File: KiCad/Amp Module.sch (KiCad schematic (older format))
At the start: 7 parts, among them J1 IDC34, J2 IDC34, J3 IDC34

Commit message: changed 4053 to DG419 & added negative latch
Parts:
- removed U?: CD4053B, symbol Analog_Switch:CD4053B
- added R? (x2): 2.2k, symbol Device:R_Small
- added R? (x2): 1k, symbol Device:R_Small
- added U? (x2): DG419, Package_SO:SOIC-8_3.9x4.9mm_P1.27mm, symbol Analog_Switch:DG419LDY
- added U? (x2): DG419LDY_Maxim, Package_SO:SOIC-8_3.9x4.9mm_P1.27mm, symbol Analog_Switch:DG419LDY_Maxim
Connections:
- wire segments 73 -> 85
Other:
- note added: "0"
- note added: "1"
- note removed: "S1=0"
- note removed: "S1=1"
- note removed: "S2=0"
- note removed: "S2=1"
- moved on the sheet: U?A, U?B, U?C

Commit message: first commit
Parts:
- removed U? (x2): DG419, Package_SO:SOIC-8_3.9x4.9mm_P1.27mm, symbol Analog_Switch:DG419LDY
- added C? (x2): 22u, symbol Device:C_Small
- added C? (x2): 22p, symbol Device:C_Small
- added R? (x2): 22K, symbol Device:R_Small
- added R? (x4): R_Small, symbol Device:R_Small
- added R? (x19): 0, symbol Device:R_Small
- added U? (x3): Opamp_Dual_Generic, symbol Device:Opamp_Dual_Generic
- added U? (x2): Rotary_SW10, symbol AmpModule:Rotary_SW10
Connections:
- wire segments 85 -> 159
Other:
- note removed: "0"
- note removed: "1"
- moved on the sheet: R?, U?A, U?B, U?C

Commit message: first single IDC commit
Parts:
- removed J3: IDC34, symbol Connector_Generic:Conn_02x17_Odd_Even
- removed U? (x2): DG419LDY_Maxim, Package_SO:SOIC-8_3.9x4.9mm_P1.27mm, symbol Analog_Switch:DG419LDY_Maxim
- removed U?: Opamp_Dual_Generic, symbol Device:Opamp_Dual_Generic
- added U? (x3): 74LS08, symbol 74xx:74LS08
- J1: value IDC34 -> DSP
- J2: value IDC34 -> LITEMOD
- U? (x2): symbol AmpModule:Rotary_SW10 -> Amp-Module-rescue:Rotary_SW10-AmpModule
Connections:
- net labels added: IOUT1MON, IOUT2MON, PROTECT1, PROTECT2, READY1, READY2, TEMPMON12, VOUT1MON, VOUT2MON
- net labels removed: DSP_IOUT1MON, DSP_IOUT2MON, DSP_PROTECT13, DSP_PROTECT24, DSP_READY13, DSP_READY24, DSP_TEMPMON12, DSP_VOUT1MON, DSP_VOUT2MON, LM_IN3+, LM_IN3-, LM_IN4+, LM_IN4-, LM_IOUT1MON, LM_IOUT2MON, LM_IOUT3MON, LM_IOUT4MON, LM_MUTE3, LM_MUTE4, LM_PROTECT1, LM_PROTECT2, LM_PROTECT3, LM_PROTECT4, LM_READY1, LM_READY2, LM_READY3, LM_READY4, LM_TEMPMON12, LM_TEMPMON34, LM_VOUT1MON, LM_VOUT2MON, LM_VOUT3MON, LM_VOUT4MON, RESERVED_A1, RESERVED_A2, RESERVED_B1, RESERVED_B2
- wire segments 159 -> 146
- no-connect marks 0 -> 4
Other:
- note added: "AUDIO"
- note added: "IDC"
- note added: "MUTE"
- note added: "TODO:\n - Check PROTECT voltage level\n - Bypass caps\n - Duplicate temp detector"
- note removed: "DSP IDC"
- note removed: "LITEMOD IDC"
- note removed: "TODO:\n - Check PROTECT voltage level\n - Bypass caps\n - VU meter"
- moved on the sheet: C?, J1, J2, R?, U?A, U?B

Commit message: freeze at 3 leds
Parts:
- removed R? (x19): 0, symbol Device:R_Small
- removed R?: R_Small, symbol Device:R_Small
- removed U? (x2): Rotary_SW10, symbol Amp-Module-rescue:Rotary_SW10-AmpModule
- added C? (x2): 22u, symbol Device:C_Small
- added R? (x2): 4.7k, symbol Device:R_Small
- added R? (x3): 18k, symbol Device:R_Small
- added R? (x2): 10k, symbol Device:R_Small
- added R? (x2): 27k, symbol Device:R_Small
- added R? (x2): 39k, symbol Device:R_Small
- added R? (x2): 53.6k, symbol Device:R_Small
- added RS? (x2): Rotary_SW07, symbol Amp-Module-rescue:Rotary_SW07
- R? (x2): value 2.2k -> 8.2k
- R? (x2): value 1k -> 2.7k
- R? (x2): value 22K -> 22k
- R? (x2): value R_Small -> 10k
- R?: value R_Small -> 18k
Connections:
- wire segments 146 -> 125
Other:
- moved on the sheet: R?, U?A, U?B

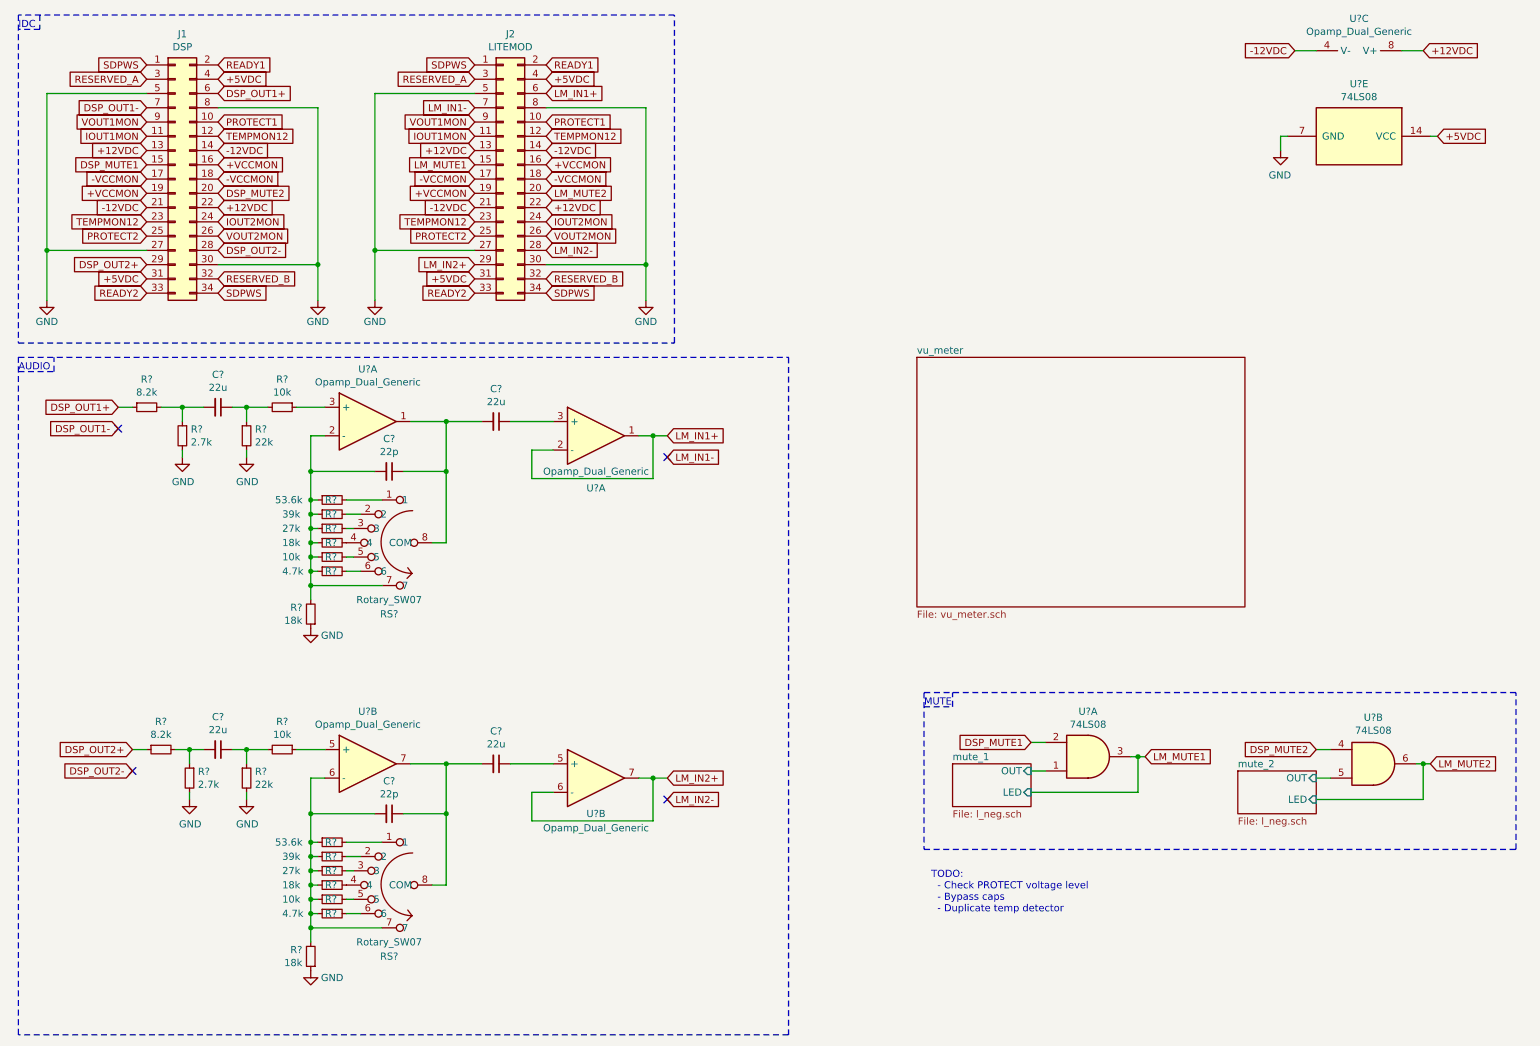
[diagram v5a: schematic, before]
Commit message: schematic completed
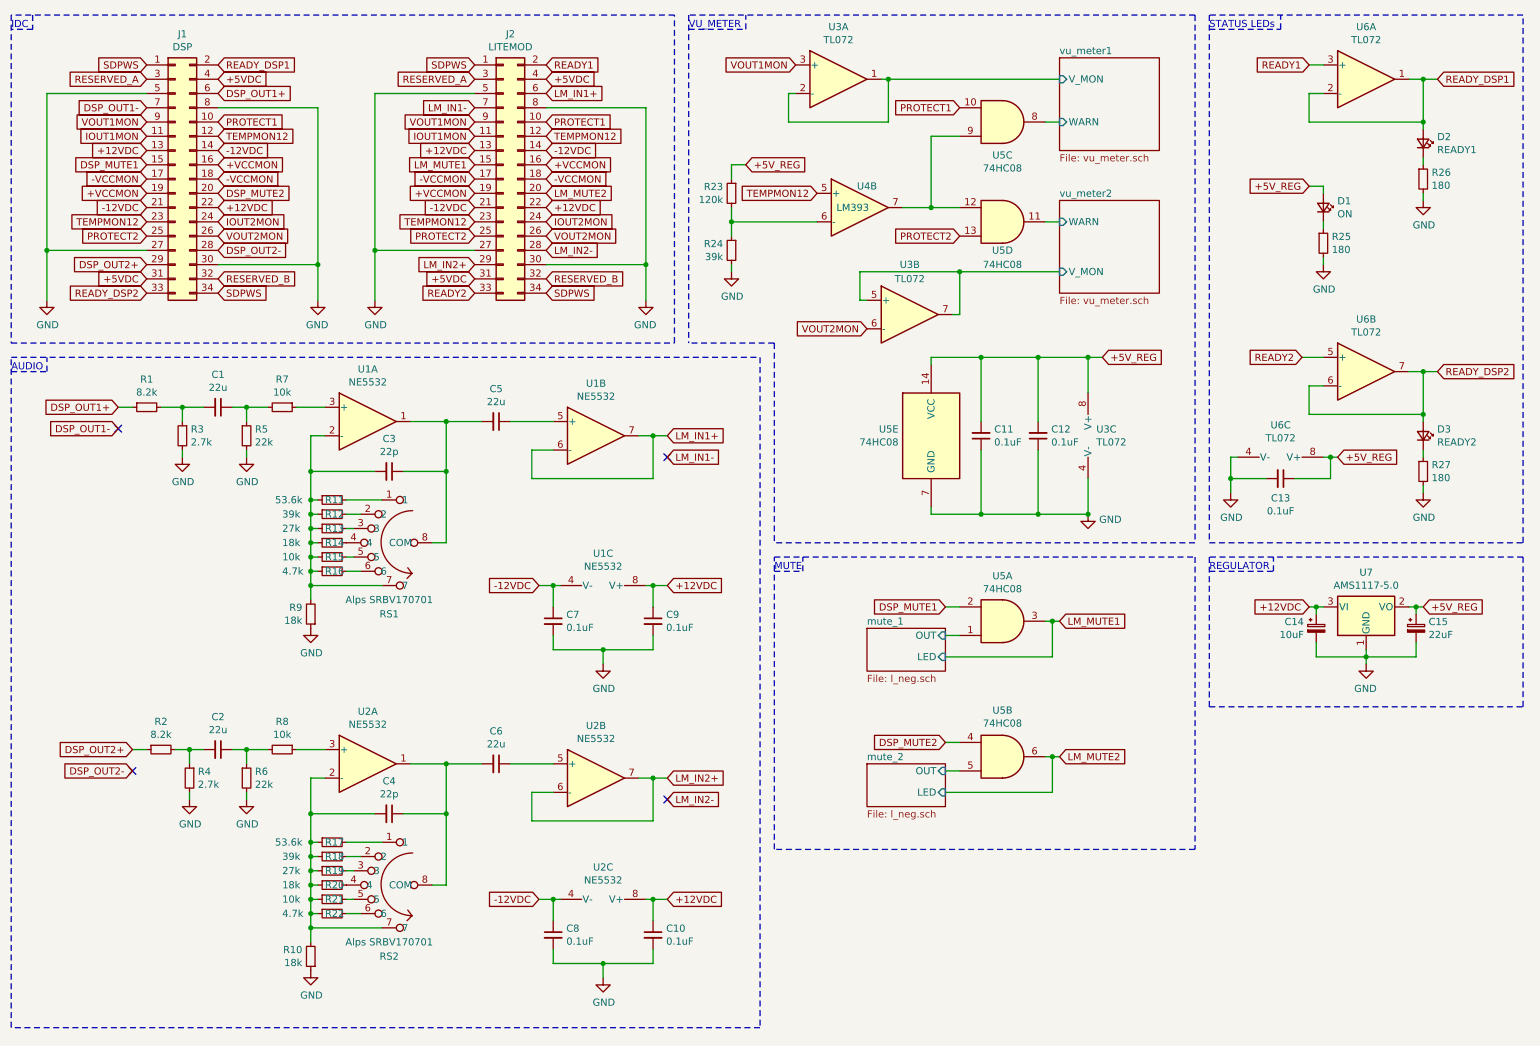
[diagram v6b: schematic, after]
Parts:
- removed U? (x5): Opamp_Dual_Generic, symbol Device:Opamp_Dual_Generic
- removed U?: 74LS08, symbol 74xx:74LS08
- added C10, C11, C12, C13, C7, C8, C9: 0.1uF, symbol Device:C_Small
- added C14: 10uF, symbol Device:CP_Small
- added C15: 22uF, symbol Device:CP_Small
- added D1: ON, symbol Device:LED_Small
- added D2: READY1, symbol Device:LED_Small
- added D3: READY2, symbol Device:LED_Small
- added R23: 120k, symbol Device:R_Small
- added R24: 39k, symbol Device:R_Small
- added R25, R26, R27: 180, symbol Device:R_Small
- added U1, U2: NE5532, symbol Amplifier_Operational:NE5532
- added U3, U6: TL072, symbol Amplifier_Operational:TL072
- added U4: LM393, symbol Amp-Module-rescue:LM393-Comparator-Amp-Module-rescue
- added unit 3 of U5
- added unit 4 of U5
- added unit 5 of U5
- added U7: AMS1117-5.0, Package_TO_SOT_SMD:SOT-223-3_TabPin2, symbol Regulator_Linear:AMS1117-5.0
- RS1, RS2: renamed from RS?; value Rotary_SW07 -> Alps SRBV170701
- U5: renamed from U?; value 74LS08 -> 74HC08
- gave numbers to parts that had none: 28
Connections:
- net +12VDC: now also C10.1, C14.1, C9.1, U1.8 (V+), U2.8 (V+), U7.3 (VI)
- net -12VDC: now also C7.1, C8.1, U1.4 (V-), U2.4 (V-)
- net GND: now also C10.2, C11.1, C12.1, C13.2, C14.2, C15.2, C7.2, C8.2, C9.2, R24.2, R25.2, R26.2, R27.2, U3.4 (V-), U5.7 (GND), U6.4 (V-), U7.1 (GND)
- net LM_IN1+: now also U1.6 (-), U1.7
- net LM_IN2+: now also U2.6 (-), U2.7
- net PROTECT1: now also U5.10
- net PROTECT2: now also U5.13
- net READY1: now also U6.3 (+); no longer J1.2 (Pin_2)
- net READY2: now also U6.5 (+); no longer J1.33 (Pin_33)
- net TEMPMON12: now also U4.5 (+)
- net VOUT1MON: now also U3.3 (+)
- net VOUT2MON: now also U3.6 (-)
- net at C5.1: now also U1.5 (+)
- net at C6.1: now also U2.5 (+)
- net at R7.1: now also U1.3 (+)
- net at C3.1, C5.2, RS1.8 (COM): now also U1.1
- net at C3.2, R11.1, R12.1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: now also U1.2 (-)
- net at R8.1: now also U2.3 (+)
- net at C4.2, R10.2, R17.1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: now also U2.2 (-)
- net at C4.1, C6.2, RS2.8 (COM): now also U2.1
- new net: D1.1 (K), R25.1
- new net: R23.2, R24.1, U4.6 (-)
- new net: U4.7, U5.12, U5.9
- new net: D2.1 (K), R26.1
- new net: D3.1 (K), R27.1
- new net +5V_REG: C11.2, C12.2, C13.1, C15.1, D1.2 (A), R23.1, U3.8 (V+), U5.14 (VCC), U6.8 (V+), U7.2 (VO)
- new net READY_DSP1: D2.2 (A), J1.2 (Pin_2), U6.1, U6.2 (-)
- new net READY_DSP2: D3.2 (A), J1.33 (Pin_33), U6.6 (-), U6.7
- new net vu_meter1/V_MON: U3.1, U3.2 (-)
- new net vu_meter1/WARN: U5.8
- new net vu_meter2/V_MON: U3.5 (+), U3.7
- new net vu_meter2/WARN: U5.11
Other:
- note added: "REGULATOR"
- note added: "STATUS LEDs"
- note added: "VU_METER"
- note removed: "TODO:\n - Check PROTECT voltage level\n - Bypass caps\n - Duplicate temp detector"
- moved on the sheet: U5A, U5B

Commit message: edited chez Gabri's
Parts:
- removed C1, C2, C5, C6: 22u, symbol Device:C_Small
- removed R10, R20: 18k, symbol Device:R_Small
- removed R17: 53.6k, symbol Device:R_Small
- removed R18: 39k, symbol Device:R_Small
- removed R19: 27k, symbol Device:R_Small
- removed R21: 10k, symbol Device:R_Small
- removed R22: 4.7k, symbol Device:R_Small
- removed R5, R6: 22k, symbol Device:R_Small
- added R? (x2): 1.8k, symbol Device:R_Small
- added R?: 1k, symbol Device:R_Small
- added R?: 2.7k, symbol Device:R_Small
- added R?: 3.9k, symbol Device:R_Small
- added R?: 5.36k, symbol Device:R_Small
- added R?: 470, symbol Device:R_Small
- R11: value 53.6k -> 5.36k
- R12: value 39k -> 3.9k
- R13: value 27k -> 2.7k
- R14, R9: value 18k -> 1.8k
- R15, R7, R8: value 10k -> 1k
- R16: value 4.7k -> 470
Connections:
- net GND: now also R?.1
- net at R1.2, R3.1: now also R7.2
- net at R2.2, R4.1: now also R8.2
- net at C3.1, RS1.8 (COM), U1.1: now also U1.5 (+)
- net at C4.1, RS2.8 (COM), U2.1: now also U2.5 (+)
- net at C4.2, RS2.7, U2.2 (-): now also R?.1, R?.1, R?.1, R?.1, R?.1, R?.1, R?.2
- net at RS2.1: now also R?.2
- net at RS2.2: now also R?.2
- net at RS2.3: now also R?.2
- net at RS2.4: now also R?.2
- net at RS2.5: now also R?.2
- net at RS2.6: now also R?.2
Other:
- note added: "check cap"
- moved on the sheet: R1, R2, R3, R4, R7, R8
